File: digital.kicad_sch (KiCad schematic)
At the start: 29 parts, among them J1 Program Connector, J2 UART, J3 LCD ILI9488, SW1 Voltage, SW2 Current, U6 REF3030, U7 STM32G431CBTx

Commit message: Dodanie obwodów odsprzęgających do przycisków enkoderów
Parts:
- added Csw1, Csw2: 100n, Capacitor_SMD:C_0805_2012Metric_Pad1.18x1.45mm_HandSolder, symbol Device:C
- added Rsw1, Rsw2: 10k, Resistor_SMD:R_0805_2012Metric_Pad1.20x1.40mm_HandSolder, symbol Device:R
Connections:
- net GNDD: now also Csw1.1, Csw2.2
- net at SW2.S2: now also Csw2.1, Rsw2.1; no longer U7.34 (PA12)
- net at U7.33 (PA11): now also Rsw1.1; no longer SW1.S2
- new net: Csw1.2, Rsw1.2, SW1.S2
- new net: Rsw2.2, U7.34 (PA12)

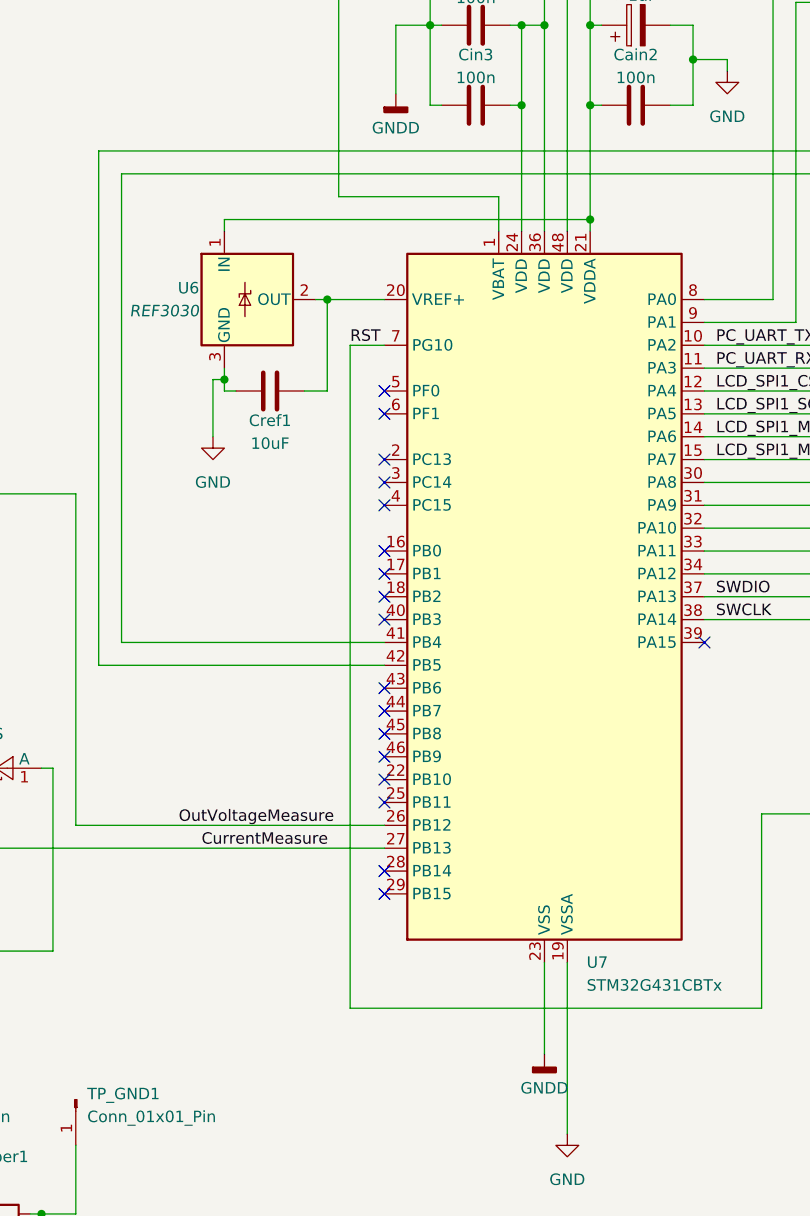
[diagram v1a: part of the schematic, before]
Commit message: walidacja schematu, dodanie footprintu do drivera, ERC
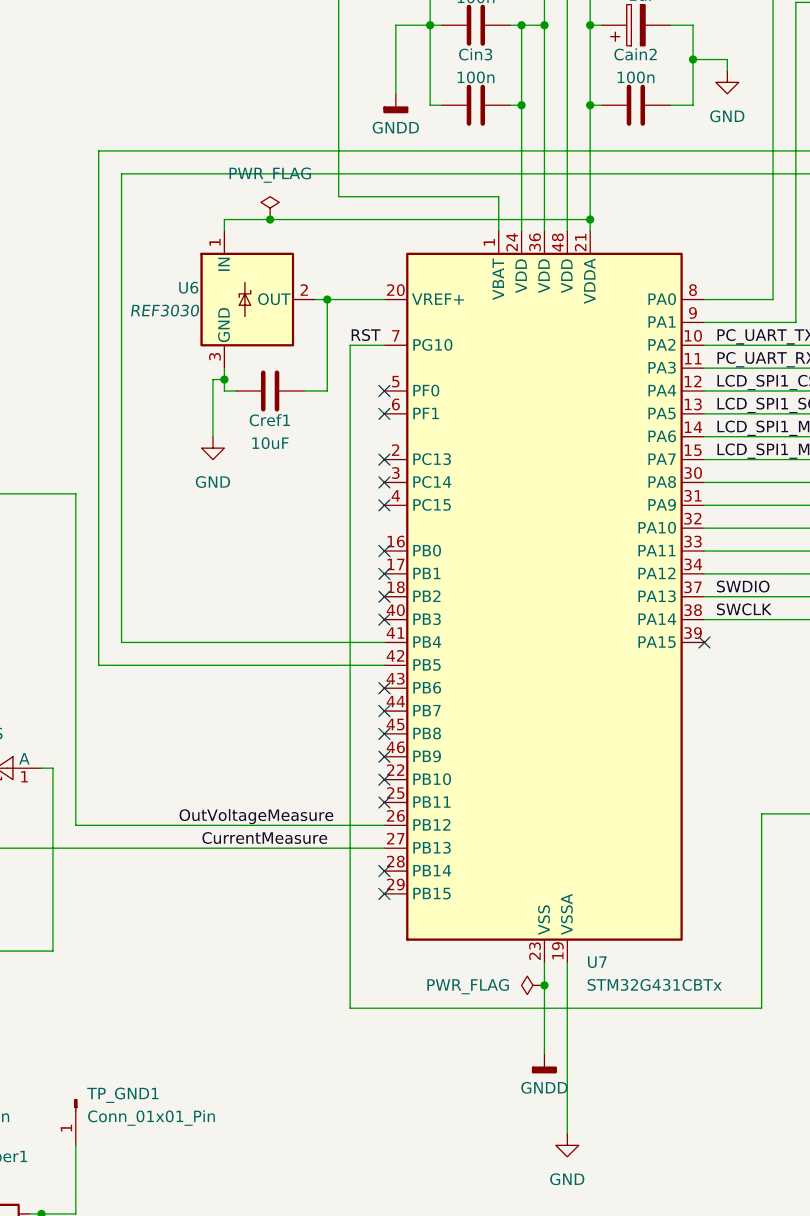
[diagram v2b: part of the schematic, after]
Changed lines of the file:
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@@
 	)
 	(junction
+		(at 113.03 58.42)
+		(diameter 0)
+		(color 0 0 0 0)
+	)
+	(junction
 		(at 140.97 36.83)
 		(diameter 0)
@@
 	)
 	(junction
+		(at 143.51 143.51)
+		(diameter 0)
+		(color 0 0 0 0)
+	)
+	(junction
 		(at 160.02 40.64)
 		(diameter 0)
@@
 	(wire
 		(pts
+			(xy 143.51 143.51) (xy 143.51 151.13)
+		)
+		(stroke
+			(width 0)
+			(type default)
+		)
+	)
+	(wire
+		(pts
 			(xy 186.69 19.05) (xy 209.55 19.05)
 		)
@@
 	(wire
 		(pts
+			(xy 113.03 58.42) (xy 148.59 58.42)
+		)
+		(stroke
+			(width 0)
+			(type default)
+		)
+	)
+	(wire
+		(pts
 			(xy 130.81 27.94) (xy 132.08 27.94)
 		)
@@
 	(wire
 		(pts
-			(xy 107.95 58.42) (xy 148.59 58.42)
+			(xy 107.95 58.42) (xy 113.03 58.42)
 		)
 		(stroke
@@
 	(wire
 		(pts
-			(xy 143.51 140.97) (xy 143.51 151.13)
+			(xy 143.51 140.97) (xy 143.51 143.51)
 		)
 		(stroke
@@
 	)
 	(symbol
+		(lib_id "power:PWR_FLAG")
+		(at 143.51 143.51 90)
+		(unit 1)
+		(body_style 1)
+		(exclude_from_sim no)
+		(in_bom yes)
+		(on_board yes)
+		(in_pos_files yes)
+		(dnp no)
+		(fields_autoplaced yes)
+		(property "Reference" "#FLG04"
+			(at 141.605 143.51 0)
+			(hide yes)
+			(show_name no)
+			(do_not_autoplace no)
+			(effects
+				(font
+					(size 1.27 1.27)
+				)
+			)
+		)
+		(property "Value" "PWR_FLAG"
+			(at 139.7 143.5099 90)
+			(show_name no)
+			(do_not_autoplace no)
+			(effects
+				(font
+					(size 1.27 1.27)
+				)
+				(justify left)
+			)
+		)
+		(property "Footprint" ""
+			(at 143.51 143.51 0)
+			(hide yes)
+			(show_name no)
+			(do_not_autoplace no)
+			(effects
+				(font
+					(size 1.27 1.27)
+				)
+			)
+		)
+		(property "Datasheet" ""
+			(at 143.51 143.51 0)
+			(hide yes)
+			(show_name no)
+			(do_not_autoplace no)
+			(effects
+				(font
+					(size 1.27 1.27)
+				)
+			)
+		)
+		(property "Description" "Special symbol for telling ERC where power comes from"
+			(at 143.51 143.51 0)
+			(hide yes)
+			(show_name no)
+			(do_not_autoplace no)
+			(effects
+				(font
+					(size 1.27 1.27)
+				)
+			)
+		)
+		(pin "1"
+		)
+		(instances
+			(project "zasilacz_projekt_kompetencyjny"
+				(path "/e9ad3936-200e-4b7c-85fb-533ca6ea54fd/eba393f9-1041-42a1-a84c-5211747d5fcc"
+					(reference "#FLG04")
+					(unit 1)
+				)
+			)
+		)
+	)
+	(symbol
 		(lib_id "Diode:BAT54S")
 		(at 80.01 119.38 0)
@@
 					(unit 1)
 				)
+			)
+		)
+	)
+	(symbol
+		(lib_id "power:PWR_FLAG")
+		(at 113.03 58.42 0)
+		(unit 1)
+		(body_style 1)
+		(exclude_from_sim no)
+		(in_bom yes)
+		(on_board yes)
+		(in_pos_files yes)
+		(dnp no)
+		(fields_autoplaced yes)
+		(property "Reference" "#FLG03"
+			(at 113.03 56.515 0)
+			(hide yes)
+			(show_name no)
+			(do_not_autoplace no)
+			(effects
+				(font
+					(size 1.27 1.27)
+				)
+			)
+		)
+		(property "Value" "PWR_FLAG"
+			(at 113.03 53.34 0)
+			(show_name no)
+			(do_not_autoplace no)
+			(effects
+				(font
+					(size 1.27 1.27)
+				)
+			)
+		)
+		(property "Footprint" ""
+			(at 113.03 58.42 0)
+			(hide yes)
+			(show_name no)
+			(do_not_autoplace no)
+			(effects
+				(font
+					(size 1.27 1.27)
+				)
+			)
+		)
+		(property "Datasheet" ""
+			(at 113.03 58.42 0)
+			(hide yes)
+			(show_name no)
+			(do_not_autoplace no)
+			(effects
+				(font
+					(size 1.27 1.27)
+				)
+			)
+		)
+		(property "Description" "Special symbol for telling ERC where power comes from"
+			(at 113.03 58.42 0)
+			(hide yes)
+			(show_name no)
+			(do_not_autoplace no)
+			(effects
+				(font
+					(size 1.27 1.27)
+				)
+			)
+		)
+		(pin "1"
+		)
+		(instances
+			(project "zasilacz_projekt_kompetencyjny"
+				(path "/e9ad3936-200e-4b7c-85fb-533ca6ea54fd/eba393f9-1041-42a1-a84c-5211747d5fcc"
+					(reference "#FLG03")
+					(unit 1)
+				)

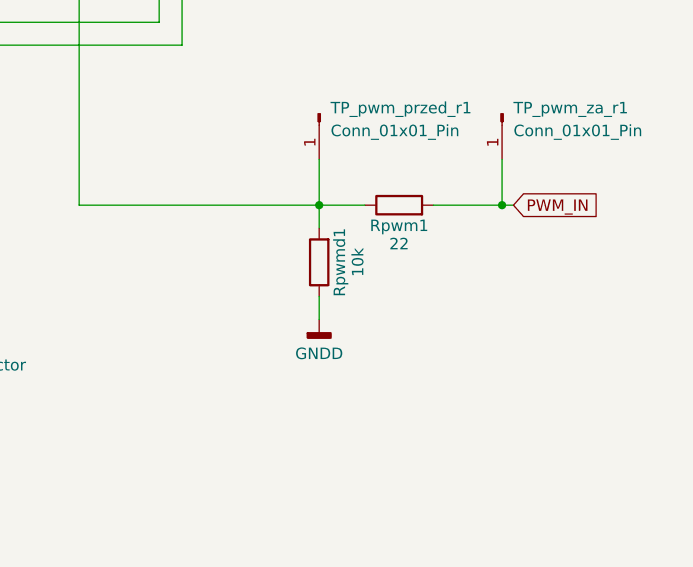
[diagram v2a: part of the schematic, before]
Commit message: Narysowanie części cyfrowej płytki, części zasialania przetwornicy głównej oraz zasilania części cyfrowej, do dokończenia połączenia mas oraz zasilań
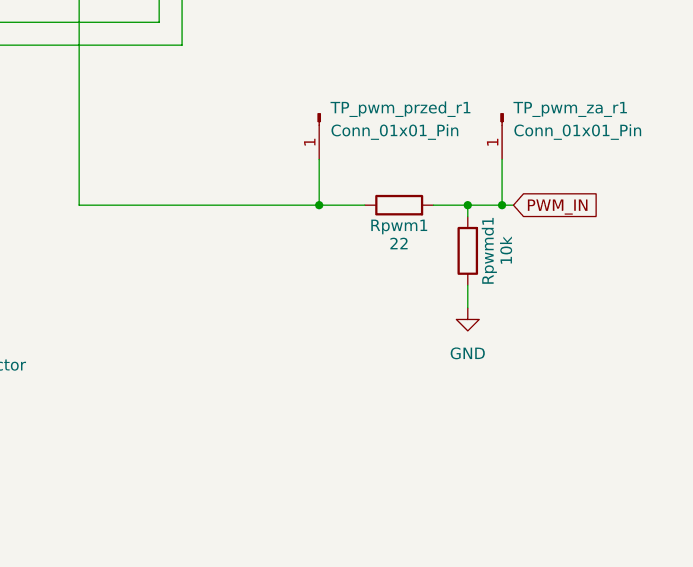
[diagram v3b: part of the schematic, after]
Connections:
- net GND: now also Rpwmd1.1
- net GNDD: no longer Rpwmd1.1
- net PWM_IN: now also Rpwmd1.2
- net at Rpwm1.1, TP_pwm_przed_r1.1 (Pin_1), U7.30 (PA8): no longer Rpwmd1.2
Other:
- moved on the sheet: Rpwmd1
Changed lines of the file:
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@@
 	)
 	(junction
+		(at 262.89 110.49)
+		(diameter 0)
+		(color 0 0 0 0)
+	)
+	(junction
 		(at 76.2 88.9)
 		(diameter 0)
@@
 	(wire
 		(pts
+			(xy 262.89 110.49) (xy 262.89 111.76)
+		)
+		(stroke
+			(width 0)
+			(type default)
+		)
+	)
+	(wire
+		(pts
 			(xy 181.61 100.33) (xy 181.61 127)
 		)
@@
 	(wire
 		(pts
-			(xy 259.08 110.49) (xy 266.7 110.49)
+			(xy 259.08 110.49) (xy 262.89 110.49)
 		)
 		(stroke
@@
 	(wire
 		(pts
+			(xy 262.89 110.49) (xy 266.7 110.49)
+		)
+		(stroke
+			(width 0)
+			(type default)
+		)
+	)
+	(wire
+		(pts
 			(xy 167.64 146.05) (xy 167.64 124.46)
 		)
@@
 	(wire
 		(pts
-			(xy 246.38 110.49) (xy 246.38 113.03)
-		)
-		(stroke
-			(width 0)
-			(type default)
-		)
-	)
-	(wire
-		(pts
 			(xy 233.68 77.47) (xy 233.68 73.66)
 		)
@@
 	(wire
 		(pts
-			(xy 246.38 120.65) (xy 246.38 123.19)
+			(xy 262.89 119.38) (xy 262.89 121.92)
 		)
 		(stroke
@@
 	)
 	(symbol
-		(lib_id "power:GNDD")
-		(at 246.38 123.19 0)
+		(lib_id "Device:C")
+		(at 113.03 77.47 90)
 		(unit 1)
 		(body_style 1)
@@
 		(in_pos_files yes)
 		(dnp no)
-		(fields_autoplaced yes)
-		(property "Reference" "#PWR028"
-			(at 246.38 129.54 0)
-			(hide yes)
+		(property "Reference" "Cref1"
+			(at 113.03 80.772 90)
 			(show_name no)
 			(do_not_autoplace no)
@@
 			)
 		)
-		(property "Value" "GNDD"
-			(at 246.38 127 0)
+		(property "Value" "10uF"
+			(at 113.03 83.312 90)
 			(show_name no)
 			(do_not_autoplace no)
@@
 			)
 		)
-		(property "Footprint" ""
-			(at 246.38 123.19 0)
+		(property "Footprint" "Capacitor_SMD:C_0805_2012Metric_Pad1.18x1.45mm_HandSolder"
+			(at 116.84 76.5048 0)
 			(hide yes)
 			(show_name no)
@@
 		)
 		(property "Datasheet" ""
-			(at 246.38 123.19 0)
+			(at 113.03 77.47 0)
 			(hide yes)
 			(show_name no)
@@
 			)
 		)
-		(property "Description" "Power symbol creates a global label with name \"GNDD\" , digital ground"
-			(at 246.38 123.19 0)
+		(property "Description" "Unpolarized capacitor"
+			(at 113.03 77.47 0)
 			(hide yes)
 			(show_name no)
@@
 		(pin "1"
 		)
+		(pin "2"
+		)
 		(instances
 			(project ""
 				(path "/c7e56cf4-6d5c-4b1f-beec-285979763629"
-					(reference "#PWR05")
+					(reference "Cref")
 					(unit 1)
 				)
@@
 			(project "zasilacz_projekt_kompetencyjny"
 				(path "/e9ad3936-200e-4b7c-85fb-533ca6ea54fd/eba393f9-1041-42a1-a84c-5211747d5fcc"
-					(reference "#PWR028")
+					(reference "Cref1")
 					(unit 1)
 				)
@@
 	)
 	(symbol
-		(lib_id "Device:C")
-		(at 113.03 77.47 90)
+		(lib_id "power:GNDD")
+		(at 209.55 29.21 0)
 		(unit 1)
 		(body_style 1)
@@
 		(in_pos_files yes)
 		(dnp no)
-		(property "Reference" "Cref1"
-			(at 113.03 80.772 90)
+		(fields_autoplaced yes)
+		(property "Reference" "#PWR026"
+			(at 209.55 35.56 0)
+			(hide yes)
 			(show_name no)
 			(do_not_autoplace no)
@@
 			)
 		)
-		(property "Value" "10uF"
-			(at 113.03 83.312 90)
+		(property "Value" "GNDD"
+			(at 209.55 33.02 0)
 			(show_name no)
 			(do_not_autoplace no)
@@
 			)
 		)
-		(property "Footprint" "Capacitor_SMD:C_0805_2012Metric_Pad1.18x1.45mm_HandSolder"
-			(at 116.84 76.5048 0)
+		(property "Footprint" ""
+			(at 209.55 29.21 0)
 			(hide yes)
 			(show_name no)
@@
 		)
 		(property "Datasheet" ""
-			(at 113.03 77.47 0)
+			(at 209.55 29.21 0)
 			(hide yes)
 			(show_name no)
@@
 			)
 		)
-		(property "Description" "Unpolarized capacitor"
-			(at 113.03 77.47 0)
+		(property "Description" "Power symbol creates a global label with name \"GNDD\" , digital ground"
+			(at 209.55 29.21 0)
 			(hide yes)
 			(show_name no)
@@
 		(pin "1"
 		)
-		(pin "2"
-		)
 		(instances
-			(project ""
+			(project "digital"
 				(path "/c7e56cf4-6d5c-4b1f-beec-285979763629"
-					(reference "Cref")
+					(reference "#PWR04")
 					(unit 1)
 				)
@@
 			(project "zasilacz_projekt_kompetencyjny"
 				(path "/e9ad3936-200e-4b7c-85fb-533ca6ea54fd/eba393f9-1041-42a1-a84c-5211747d5fcc"
-					(reference "Cref1")
+					(reference "#PWR026")
 					(unit 1)
 				)
@@
 	)
 	(symbol
-		(lib_id "power:GNDD")
-		(at 209.55 29.21 0)
+		(lib_id "power:GND")
+		(at 262.89 121.92 0)
 		(unit 1)
 		(body_style 1)
@@
 		(dnp no)
 		(fields_autoplaced yes)
-		(property "Reference" "#PWR026"
-			(at 209.55 35.56 0)
+		(property "Reference" "#PWR028"
+			(at 262.89 128.27 0)
 			(hide yes)
 			(show_name no)
@@
 			)
 		)
-		(property "Value" "GNDD"
-			(at 209.55 33.02 0)
+		(property "Value" "GND"
+			(at 262.89 127 0)
 			(show_name no)
 			(do_not_autoplace no)
@@
 		)
 		(property "Footprint" ""
-			(at 209.55 29.21 0)
+			(at 262.89 121.92 0)
 			(hide yes)
 			(show_name no)
@@
 		)
 		(property "Datasheet" ""
-			(at 209.55 29.21 0)
+			(at 262.89 121.92 0)
 			(hide yes)
 			(show_name no)
@@
 			)
 		)
-		(property "Description" "Power symbol creates a global label with name \"GNDD\" , digital ground"
-			(at 209.55 29.21 0)
+		(property "Description" "Power symbol creates a global label with name \"GND\" , ground"
+			(at 262.89 121.92 0)
 			(hide yes)
 			(show_name no)
@@
 		)
 		(instances
-			(project "digital"
-				(path "/c7e56cf4-6d5c-4b1f-beec-285979763629"
-					(reference "#PWR04")
-					(unit 1)
-				)
-			)
 			(project "zasilacz_projekt_kompetencyjny"
 				(path "/e9ad3936-200e-4b7c-85fb-533ca6ea54fd/eba393f9-1041-42a1-a84c-5211747d5fcc"
-					(reference "#PWR026")
+					(reference "#PWR028")
 					(unit 1)
 				)
@@
 	(symbol
 		(lib_id "Device:R")
-		(at 246.38 116.84 180)
+		(at 262.89 115.57 180)
 		(unit 1)
 		(body_style 1)
@@
 		(dnp no)
 		(property "Reference" "Rpwmd1"
-			(at 248.666 116.84 90)
+			(at 265.176 115.57 90)
 			(show_name no)
 			(do_not_autoplace no)
@@
 		)
 		(property "Value" "10k"
-			(at 250.698 116.84 90)
+			(at 267.208 115.57 90)
 			(show_name no)
 			(do_not_autoplace no)
@@
 		)
 		(property "Footprint" "Resistor_SMD:R_0805_2012Metric_Pad1.20x1.40mm_HandSolder"
-			(at 248.158 116.84 90)
+			(at 264.668 115.57 90)
 			(hide yes)
 			(show_name no)
@@
 		)
 		(property "Datasheet" ""
-			(at 246.38 116.84 0)
+			(at 262.89 115.57 0)
 			(hide yes)
 			(show_name no)
@@
 		)
 		(property "Description" "Resistor"
-			(at 246.38 116.84 0)
+			(at 262.89 115.57 0)
 			(hide yes)
 			(show_name no)
@@
 		)
 	)
-	(embedded_fonts no)
 )

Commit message: zakończenie projektu pcb
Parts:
- removed TP_GND1, TP_GNDD1: Conn_01x01_Pin, Connector_PinHeader_2.54mm:PinHeader_1x01_P2.54mm_Vertical, symbol Connector:Conn_01x01_Pin
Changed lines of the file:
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@@
 	)
 	(junction
-		(at 87.63 168.91)
-		(diameter 0)
-		(color 0 0 0 0)
-	)
-	(junction
 		(at 262.89 110.49)
 		(diameter 0)
@@
 	)
 	(junction
-		(at 77.47 168.91)
-		(diameter 0)
-		(color 0 0 0 0)
-	)
-	(junction
 		(at 71.12 101.6)
 		(diameter 0)
@@
 	(wire
 		(pts
-			(xy 91.44 168.91) (xy 87.63 168.91)
-		)
-		(stroke
-			(width 0)
-			(type default)
-		)
-	)
-	(wire
-		(pts
 			(xy 219.71 87.63) (xy 219.71 110.49)
 		)
@@
 	(wire
 		(pts
-			(xy 91.44 161.29) (xy 91.44 168.91)
-		)
-		(stroke
-			(width 0)
-			(type default)
-		)
-	)
-	(wire
-		(pts
 			(xy 76.2 88.9) (xy 76.2 91.44)
 		)
@@
 	(wire
 		(pts
-			(xy 77.47 161.29) (xy 77.47 168.91)
-		)
-		(stroke
-			(width 0)
-			(type default)
-		)
-	)
-	(wire
-		(pts
 			(xy 148.59 36.83) (xy 148.59 45.72)
 		)
@@
 	(wire
 		(pts
-			(xy 68.58 161.29) (xy 77.47 161.29)
-		)
-		(stroke
-			(width 0)
-			(type default)
-		)
-	)
-	(wire
-		(pts
 			(xy 189.23 29.21) (xy 168.91 29.21)
 		)
@@
 	)
 	(symbol
-		(lib_id "Connector:Conn_01x01_Pin")
-		(at 91.44 156.21 270)
-		(unit 1)
-		(body_style 1)
-		(exclude_from_sim no)
-		(in_bom yes)
-		(on_board yes)
-		(in_pos_files yes)
-		(dnp no)
-		(fields_autoplaced yes)
-		(property "Reference" "TP_GND1"
-			(at 92.71 155.5749 90)
-			(show_name no)
-			(do_not_autoplace no)
-			(effects
-				(font
-					(size 1.27 1.27)
-				)
-				(justify left)
-			)
-		)
-		(property "Value" "Conn_01x01_Pin"
-			(at 92.71 158.1149 90)
-			(show_name no)
-			(do_not_autoplace no)
-			(effects
-				(font
-					(size 1.27 1.27)
-				)
-				(justify left)
-			)
-		)
-		(property "Footprint" "Connector_PinHeader_2.54mm:PinHeader_1x01_P2.54mm_Vertical"
-			(at 91.44 156.21 0)
-			(hide yes)
-			(show_name no)
-			(do_not_autoplace no)
-			(effects
-				(font
-					(size 1.27 1.27)
-				)
-			)
-		)
-		(property "Datasheet" ""
-			(at 91.44 156.21 0)
-			(hide yes)
-			(show_name no)
-			(do_not_autoplace no)
-			(effects
-				(font
-					(size 1.27 1.27)
-				)
-			)
-		)
-		(property "Description" "Generic connector, single row, 01x01, script generated"
-			(at 91.44 156.21 0)
-			(hide yes)
-			(show_name no)
-			(do_not_autoplace no)
-			(effects
-				(font
-					(size 1.27 1.27)
-				)
-			)
-		)
-		(pin "1"
-		)
-		(instances
-			(project "zasilacz_projekt_kompetencyjny"
-				(path "/e9ad3936-200e-4b7c-85fb-533ca6ea54fd/eba393f9-1041-42a1-a84c-5211747d5fcc"
-					(reference "TP_GND1")
-					(unit 1)
-				)
-			)
-		)
-	)
-	(symbol
 		(lib_id "power:GNDD")
 		(at 77.47 171.45 0)
@@
 	)
 	(symbol
-		(lib_id "Connector:Conn_01x01_Pin")
-		(at 68.58 156.21 270)
-		(unit 1)
-		(body_style 1)
-		(exclude_from_sim no)
-		(in_bom yes)
-		(on_board yes)
-		(in_pos_files yes)
-		(dnp no)
-		(fields_autoplaced yes)
-		(property "Reference" "TP_GNDD1"
-			(at 69.85 155.5749 90)
-			(show_name no)
-			(do_not_autoplace no)
-			(effects
-				(font
-					(size 1.27 1.27)
-				)
-				(justify left)
-			)
-		)
-		(property "Value" "Conn_01x01_Pin"
-			(at 69.85 158.1149 90)
-			(show_name no)
-			(do_not_autoplace no)
-			(effects
-				(font
-					(size 1.27 1.27)
-				)
-				(justify left)
-			)
-		)
-		(property "Footprint" "Connector_PinHeader_2.54mm:PinHeader_1x01_P2.54mm_Vertical"
-			(at 68.58 156.21 0)
-			(hide yes)
-			(show_name no)
-			(do_not_autoplace no)
-			(effects
-				(font
-					(size 1.27 1.27)
-				)
-			)
-		)
-		(property "Datasheet" ""
-			(at 68.58 156.21 0)
-			(hide yes)
-			(show_name no)
-			(do_not_autoplace no)
-			(effects
-				(font
-					(size 1.27 1.27)
-				)
-			)
-		)
-		(property "Description" "Generic connector, single row, 01x01, script generated"
-			(at 68.58 156.21 0)
-			(hide yes)
-			(show_name no)
-			(do_not_autoplace no)
-			(effects
-				(font
-					(size 1.27 1.27)
-				)
-			)
-		)
-		(pin "1"
-		)
-		(instances
-			(project "zasilacz_projekt_kompetencyjny"
-				(path "/e9ad3936-200e-4b7c-85fb-533ca6ea54fd/eba393f9-1041-42a1-a84c-5211747d5fcc"
-					(reference "TP_GNDD1")
-					(unit 1)
-				)
-			)
-		)
-	)
-	(symbol
 		(lib_id "Connector:Conn_01x09_Pin")
 		(at 246.38 68.58 180)
@@
 		)
 	)
+	(embedded_fonts no)
 )
